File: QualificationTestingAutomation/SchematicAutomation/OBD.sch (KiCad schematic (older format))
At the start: 0 parts

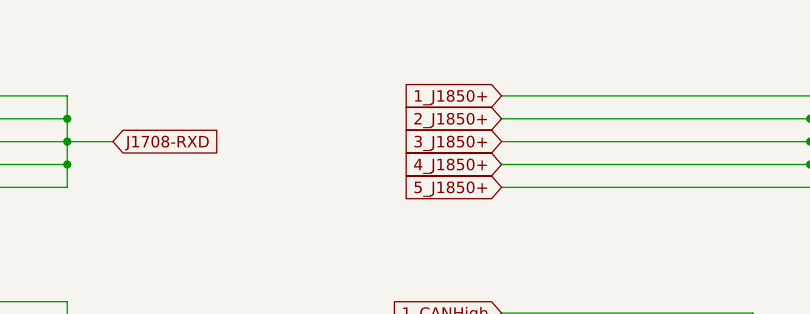
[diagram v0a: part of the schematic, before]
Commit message: CLEANED UP THE SCHEMATICS ADDED NEADED FIXES FOUND ON THE BOARD
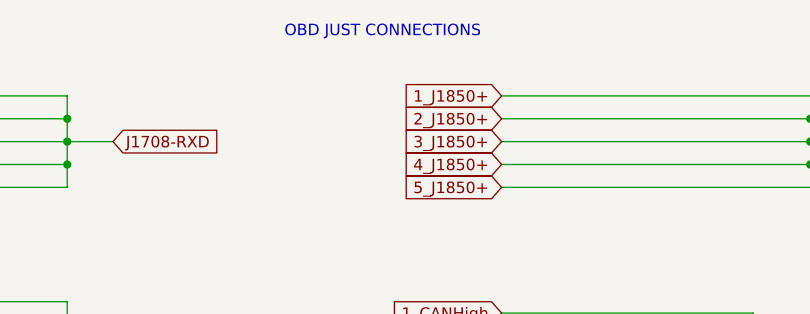
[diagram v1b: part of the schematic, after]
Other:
- note added: "OBD JUST CONNECTIONS"
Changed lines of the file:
@@
 Wire Wire Line
 	5450 7250 5450 7150
+Text Notes 3150 6700 0    50   ~ 0
+OBD JUST CONNECTIONS
 $EndSCHEMATC
